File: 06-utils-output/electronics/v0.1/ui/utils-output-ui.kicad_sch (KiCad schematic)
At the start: 31 parts, among them J1 Conn_02x03_Odd_Even, J2 Conn_02x04_Odd_Even, J3 Conn_02x02_Odd_Even, J4 Conn_01x02, J5 Conn_01x06, J6 Conn_02x05_Odd_Even, Q1 2N3904

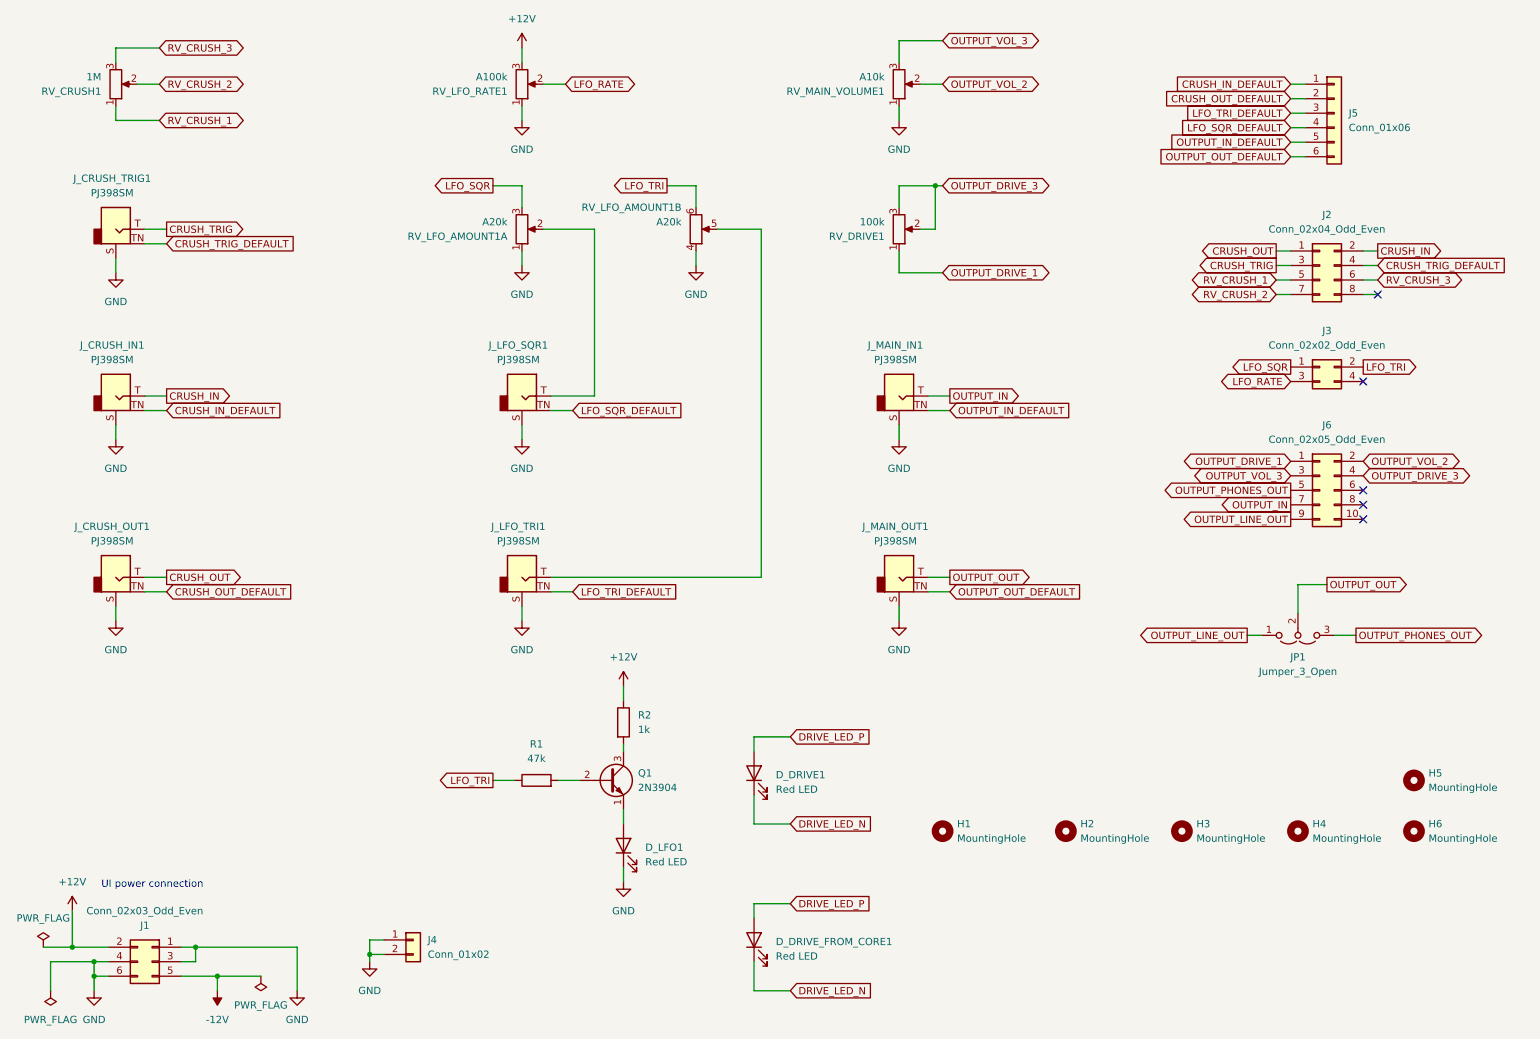
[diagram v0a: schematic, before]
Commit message: Started swapping output and bitcrusher positions
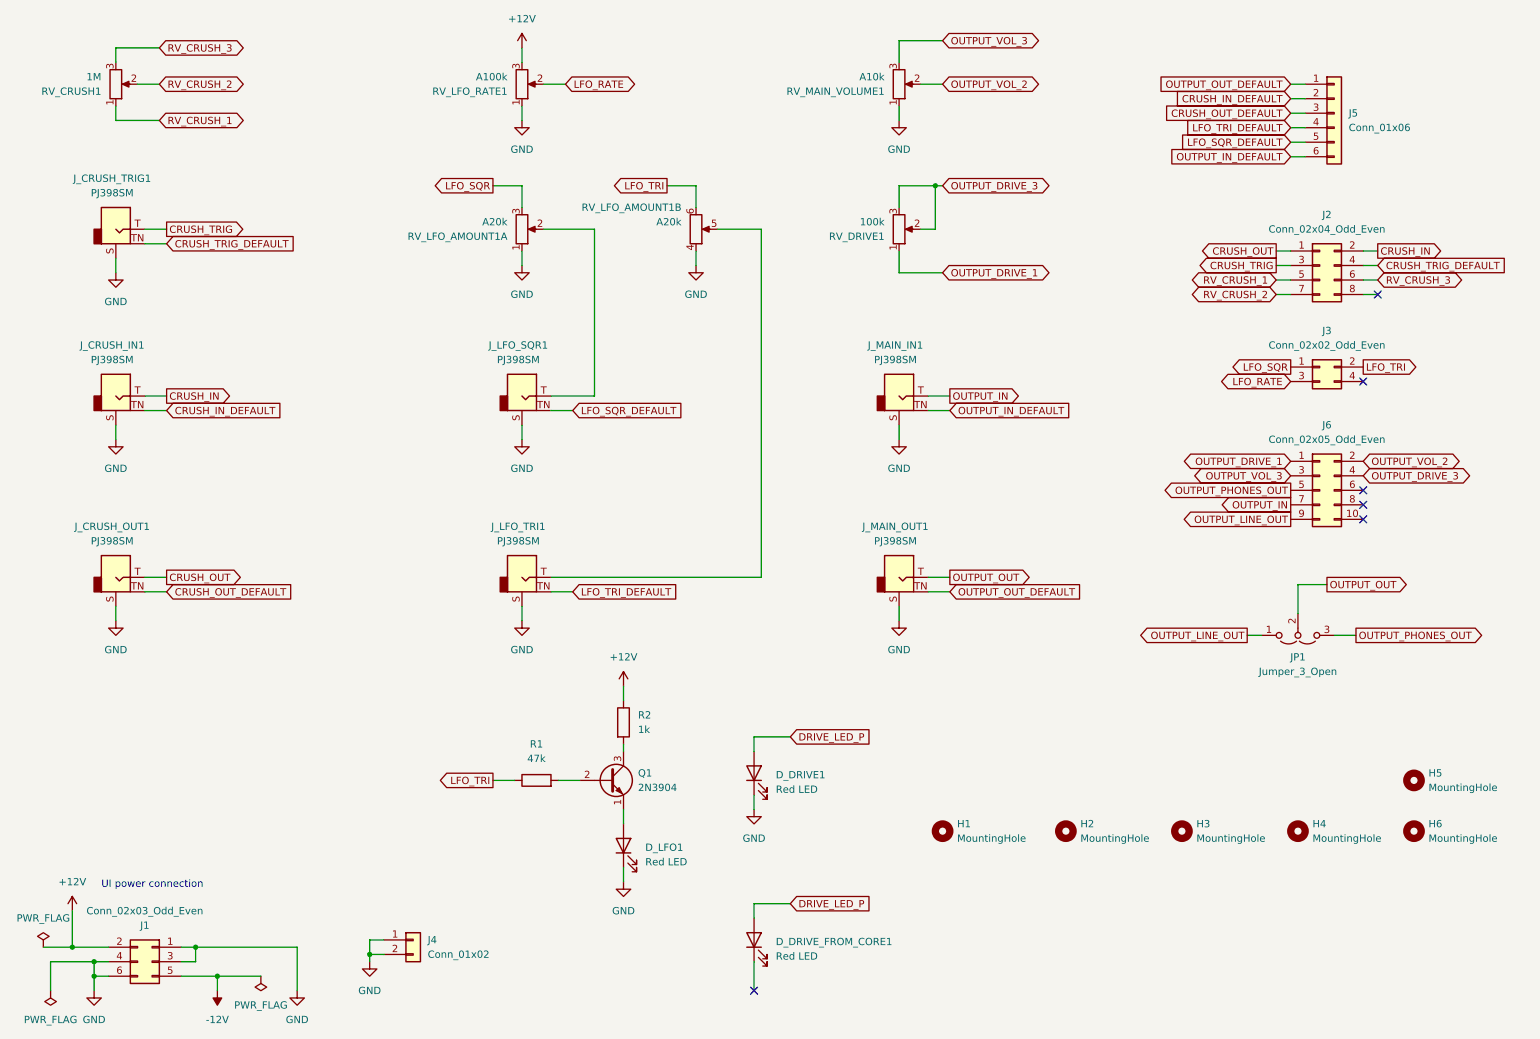
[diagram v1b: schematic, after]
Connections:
- net CRUSH_IN_DEFAULT: now also J5.2 (Pin_2); no longer J5.1 (Pin_1)
- net CRUSH_OUT_DEFAULT: now also J5.3 (Pin_3); no longer J5.2 (Pin_2)
- net GND: now also D_DRIVE1.1 (K)
- net LFO_SQR_DEFAULT: now also J5.5 (Pin_5); no longer J5.4 (Pin_4)
- net LFO_TRI_DEFAULT: now also J5.4 (Pin_4); no longer J5.3 (Pin_3)
- net OUTPUT_IN_DEFAULT: now also J5.6 (Pin_6); no longer J5.5 (Pin_5)
- net OUTPUT_OUT_DEFAULT: now also J5.1 (Pin_1); no longer J5.6 (Pin_6)
- net DRIVE_LED_N: no longer names the net of D_DRIVE_FROM_CORE1.1 (K)
- net DRIVE_LED_N: no longer D_DRIVE1.1 (K)
- no-connect marks 5 -> 6
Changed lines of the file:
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@@
+	)
+	(no_connect
+		(at 146.05 187.96)
 	)
 	(no_connect
@@
 	(wire
 		(pts
-			(xy 146.05 158.75) (xy 146.05 153.67)
-		)
-		(stroke
-			(width 0)
-			(type default)
-		)
-	)
-	(wire
-		(pts
 			(xy 39.37 54.61) (xy 43.18 54.61)
 		)
@@
 	(wire
 		(pts
-			(xy 146.05 158.75) (xy 152.4 158.75)
-		)
-		(stroke
-			(width 0)
-			(type default)
-		)
-	)
-	(wire
-		(pts
 			(xy 105.41 120.65) (xy 105.41 123.19)
 		)
@@
 	(wire
 		(pts
+			(xy 146.05 156.21) (xy 146.05 153.67)
+		)
+		(stroke
+			(width 0)
+			(type default)
+		)
+	)
+	(wire
+		(pts
 			(xy 240.03 39.37) (xy 242.57 39.37)
 		)
@@
 		(pts
 			(xy 179.07 62.23) (xy 171.45 62.23)
-		)
-		(stroke
-			(width 0)
-			(type default)
-		)
-	)
-	(wire
-		(pts
-			(xy 146.05 187.96) (xy 152.4 187.96)
 		)
 		(stroke
@@
 	(global_label "OUTPUT_OUT_DEFAULT"
 		(shape input)
-		(at 240.03 41.91 180)
+		(at 240.03 29.21 180)
 		(fields_autoplaced yes)
 		(effects
@@
 		)
 		(property "Intersheetrefs" "${INTERSHEET_REFS}"
-			(at 216.3619 41.91 0)
+			(at 216.3619 29.21 0)
 			(effects
 				(font
@@
 	(global_label "LFO_SQR_DEFAULT"
 		(shape input)
-		(at 240.03 36.83 180)
+		(at 240.03 39.37 180)
 		(fields_autoplaced yes)
 		(effects
@@
 		)
 		(property "Intersheetrefs" "${INTERSHEET_REFS}"
-			(at 219.93 36.83 0)
+			(at 219.93 39.37 0)
 			(effects
 				(font
@@
 	(global_label "CRUSH_OUT_DEFAULT"
 		(shape input)
-		(at 240.03 31.75 180)
+		(at 240.03 34.29 180)
 		(fields_autoplaced yes)
 		(effects
@@
 		)
 		(property "Intersheetrefs" "${INTERSHEET_REFS}"
-			(at 217.1481 31.75 0)
+			(at 217.1481 34.29 0)
 			(effects
 				(font
@@
 		)
 	)
-	(global_label "DRIVE_LED_N"
-		(shape input)
-		(at 152.4 187.96 0)
-		(fields_autoplaced yes)
-		(effects
-			(font
-				(size 1.27 1.27)
-			)
-			(justify left)
-		)
-		(property "Intersheetrefs" "${INTERSHEET_REFS}"
-			(at 167.4804 187.96 0)
-			(effects
-				(font
-					(size 1.27 1.27)
-				)
-				(justify left)
-				(hide yes)
-			)
-		)
-	)
 	(global_label "CRUSH_IN_DEFAULT"
 		(shape input)
@@
 	(global_label "LFO_TRI_DEFAULT"
 		(shape input)
-		(at 240.03 34.29 180)
+		(at 240.03 36.83 180)
 		(fields_autoplaced yes)
 		(effects
@@
 		)
 		(property "Intersheetrefs" "${INTERSHEET_REFS}"
-			(at 220.8976 34.29 0)
+			(at 220.8976 36.83 0)
 			(effects
 				(font
@@
 				)
 				(justify right)
-				(hide yes)
-			)
-		)
-	)
-	(global_label "DRIVE_LED_N"
-		(shape input)
-		(at 152.4 158.75 0)
-		(fields_autoplaced yes)
-		(effects
-			(font
-				(size 1.27 1.27)
-			)
-			(justify left)
-		)
-		(property "Intersheetrefs" "${INTERSHEET_REFS}"
-			(at 167.4804 158.75 0)
-			(effects
-				(font
-					(size 1.27 1.27)
-				)
-				(justify left)
 				(hide yes)
 			)
@@
 	(global_label "OUTPUT_IN_DEFAULT"
 		(shape input)
-		(at 240.03 39.37 180)
+		(at 240.03 41.91 180)
 		(fields_autoplaced yes)
 		(effects
@@
 		)
 		(property "Intersheetrefs" "${INTERSHEET_REFS}"
-			(at 218.0552 39.37 0)
+			(at 218.0552 41.91 0)
 			(effects
 				(font
@@
 	(global_label "CRUSH_IN_DEFAULT"
 		(shape input)
-		(at 240.03 29.21 180)
+		(at 240.03 31.75 180)
 		(fields_autoplaced yes)
 		(effects
@@
 		)
 		(property "Intersheetrefs" "${INTERSHEET_REFS}"
-			(at 218.8414 29.21 0)
+			(at 218.8414 31.75 0)
 			(effects
 				(font
@@
 					(unit 1)
 				)
+			)
+		)
+	)
+	(symbol
+		(lib_id "power:GND")
+		(at 146.05 156.21 0)
+		(unit 1)
+		(exclude_from_sim no)
+		(in_bom yes)
+		(on_board yes)
+		(dnp no)
+		(fields_autoplaced yes)
+		(property "Reference" "#PWR019"
+			(at 146.05 162.56 0)
+			(effects
+				(font
+					(size 1.27 1.27)
+				)
+				(hide yes)
+			)
+		)
+		(property "Value" "GND"
+			(at 146.05 161.29 0)
+			(effects
+				(font
+					(size 1.27 1.27)
+				)
+			)
+		)
+		(property "Footprint" ""
+			(at 146.05 156.21 0)
+			(effects
+				(font
+					(size 1.27 1.27)
+				)
+				(hide yes)
+			)
+		)
+		(property "Datasheet" ""
+			(at 146.05 156.21 0)
+			(effects
+				(font
+					(size 1.27 1.27)
+				)
+				(hide yes)
+			)
+		)
+		(property "Description" "Power symbol creates a global label with name \"GND\" , ground"
+			(at 146.05 156.21 0)
+			(effects
+				(font
+					(size 1.27 1.27)
+				)
+				(hide yes)
+			)
+		)
+		(pin "1"
+		)
+		(instances
+			(project ""
+				(path "/ab333f71-eefa-415f-b212-ebe7a942b1c8"
+					(reference "#PWR019")
+					(unit 1)
+				)
